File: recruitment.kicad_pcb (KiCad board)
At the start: 2 copper layers, 1 part

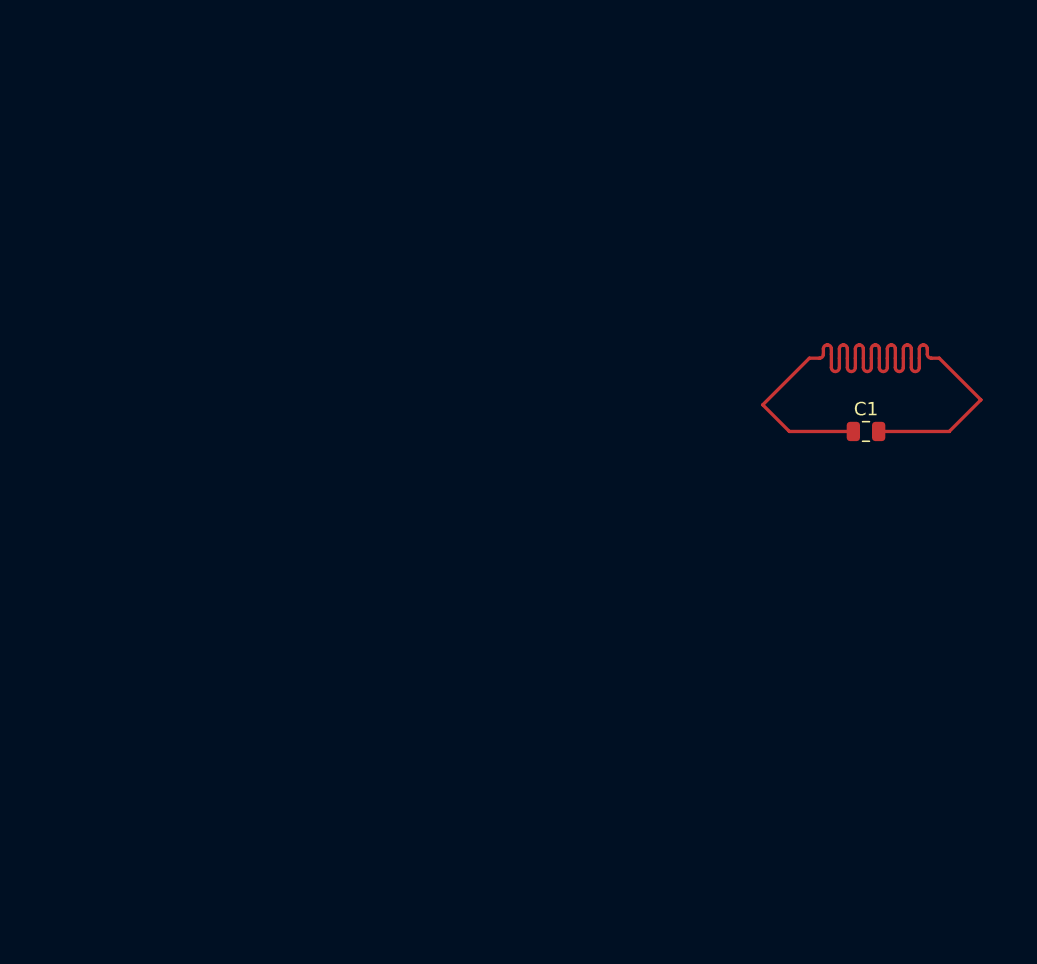
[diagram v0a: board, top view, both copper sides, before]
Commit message: TODO: ad633 footprint
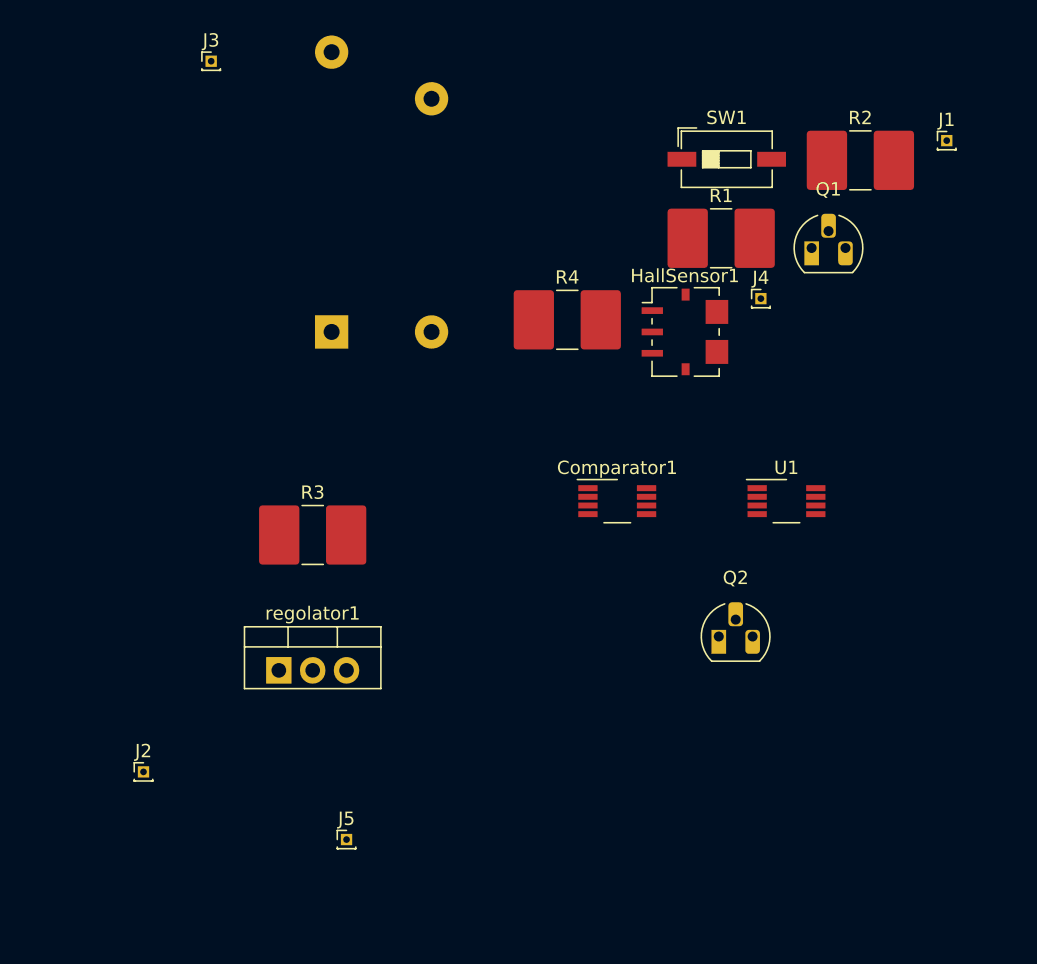
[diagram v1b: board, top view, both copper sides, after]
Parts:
- removed C1: 1F, Capacitor_SMD:C_0805_2012Metric
- added Comparator1: LM393, Package_SO:VSSOP-8_3.0x3.0mm_P0.65mm, F.Cu at (132.1, 94.0)
- added HallSensor1: Allegro ACS781xLR, Sensor_Current:Allegro_PSOF-7_4.8x6.4mm_P1.60mm, F.Cu at (137.2, 81.3)
- added J1: Conn_01x01_Female, Connector_PinHeader_1.00mm:PinHeader_1x01_P1.00mm_Vertical, F.Cu at (156.8, 66.9)
- added J2: Conn_01x01_Female, Connector_PinHeader_1.00mm:PinHeader_1x01_P1.00mm_Vertical, F.Cu at (96.5, 114.3)
- added J3: Conn_01x01_Female, Connector_PinHeader_1.00mm:PinHeader_1x01_P1.00mm_Vertical, F.Cu at (101.6, 61.0)
- added J4: Conn_01x01_Female, Connector_PinHeader_1.00mm:PinHeader_1x01_P1.00mm_Vertical, F.Cu at (142.9, 78.8)
- added J5: Conn_01x01_Female, Connector_PinHeader_1.00mm:PinHeader_1x01_P1.00mm_Vertical, F.Cu at (111.8, 119.4)
- added K1: relay, Relay_THT:Relay_1P1T_NO_10x24x18.8mm_Panasonic_ADW11xxxxW_THT, B.Cu at (110.6, 81.3)
- added Q1: Q_NPN_BCE, Package_TO_SOT_THT:TO-92_HandSolder, F.Cu at (146.7, 75.0)
- added Q2: Q_NPN_BCE, Package_TO_SOT_THT:TO-92_HandSolder, F.Cu at (139.7, 104.1)
- added R1: 1150, Resistor_SMD:R_2816_7142Metric, F.Cu at (139.9, 74.2)
- added R2: 1000, Resistor_SMD:R_2816_7142Metric, F.Cu at (150.3, 68.4)
- added R3: R, Resistor_SMD:R_2816_7142Metric, F.Cu at (109.2, 96.5)
- added R4: R, Resistor_SMD:R_2816_7142Metric, F.Cu at (128.3, 80.4)
- added SW1: SW_SPST, Button_Switch_SMD:SW_DIP_SPSTx01_Slide_6.7x4.1mm_W6.73mm_P2.54mm_LowProfile_JPin, F.Cu at (140.3, 68.3)
- added U1: LM393, Package_SO:VSSOP-8_3.0x3.0mm_P0.65mm, F.Cu at (144.8, 94.0)
- added regolator1: 5V, Package_TO_SOT_THT:TO-220-3_Vertical, F.Cu at (106.7, 106.7)
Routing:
- net Net-(C1-Pad1): track 57.5 -> 0.00 mm

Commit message: footprints/autorouting done, TODO: understand transistor and optimize pcb shape
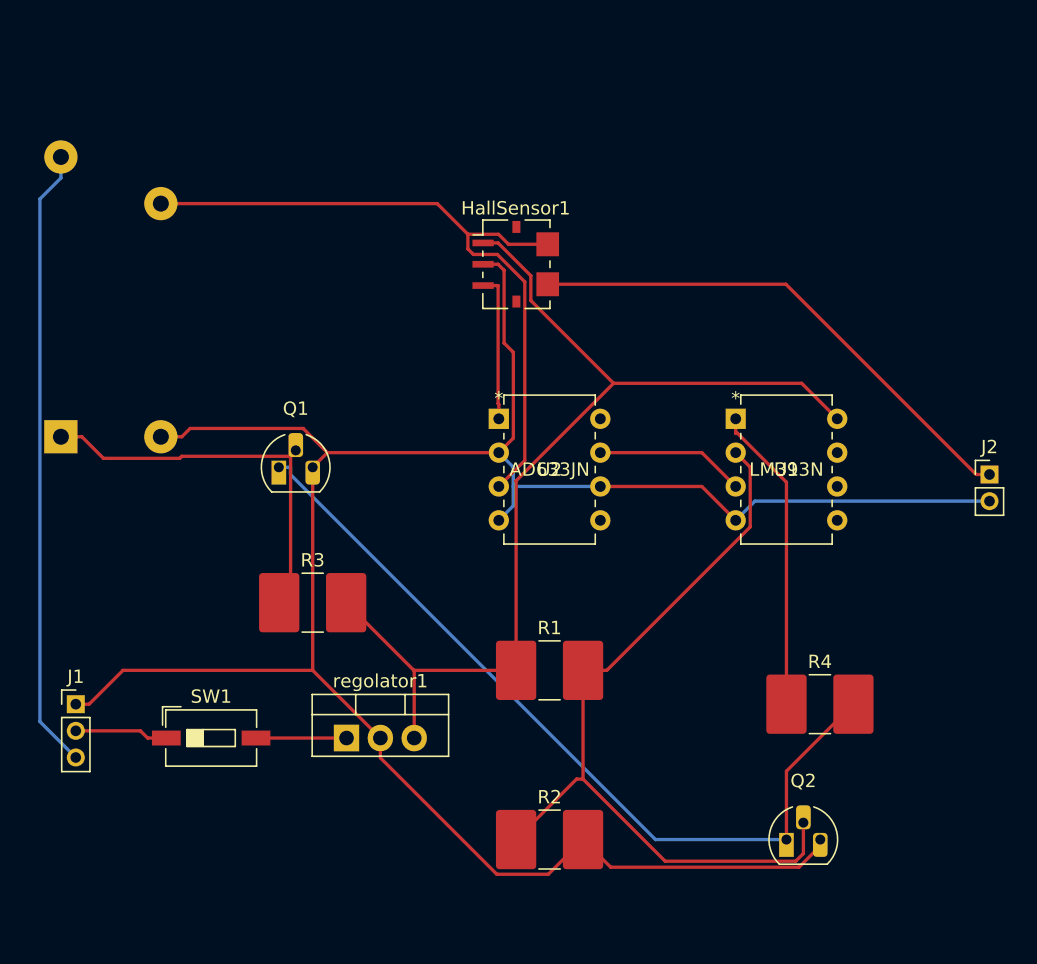
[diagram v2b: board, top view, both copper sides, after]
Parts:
- removed Comparator1: LM393, Package_SO:VSSOP-8_3.0x3.0mm_P0.65mm
- removed J3, J4, J5: Conn_01x01_Female, Connector_PinHeader_1.00mm:PinHeader_1x01_P1.00mm_Vertical
- added U2: AD633JN, LM393:LM393N, F.Cu at (123.2, 87.8)
- J1: value Conn_01x01_Female -> Conn_01x03_Female; footprint Connector_PinHeader_1.00mm:PinHeader_1x01_P1.00mm_Vertical -> Connector_PinHeader_2.00mm:PinHeader_1x03_P2.00mm_Vertical
- J2: value Conn_01x01_Female -> Conn_01x02_Female; footprint Connector_PinHeader_1.00mm:PinHeader_1x01_P1.00mm_Vertical -> Connector_PinHeader_2.00mm:PinHeader_1x02_P2.00mm_Vertical
- U1: value LM393 -> LM393N; footprint Package_SO:VSSOP-8_3.0x3.0mm_P0.65mm -> LM393:LM393N
- moved J1 77.9 mm to (91.4, 109.2)
- moved J2 67.3 mm to (160.0, 92.0)
- moved SW1 58.2 mm to (101.6, 111.8)
- moved R2 56.1 mm to (127.0, 119.4)
- moved Q1 43.2 mm to (106.7, 91.4)
- moved R1 34.9 mm to (127.0, 106.7)
- moved R4 34.5 mm to (147.3, 109.2)
- moved K1 21.8 mm to (90.3, 89.1)
- moved Q2 16.1 mm to (144.8, 119.4)
- moved HallSensor1 13.7 mm to (124.5, 76.2)
- moved U1 7.26 mm to (141.0, 87.8)
- moved regolator1 7.18 mm to (111.8, 111.8)
- moved R3 5.08 mm to (109.2, 101.6)
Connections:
- J1 pad 1: Net-(J1-Pad1) -> GND
- J2 pad 1: GND -> Net-(HallSensor1-Pad5)
- K1 pad 3: Net-(J3-Pad1) -> Net-(J1-Pad3)
- Q2 pad 2: Net-(Comparator1-Pad2) -> Net-(Q2-Pad2)
- R1 pad 2: Net-(Comparator1-Pad2) -> Net-(Q2-Pad2)
- R2 pad 1: Net-(Comparator1-Pad2) -> Net-(Q2-Pad2)
- SW1 pad 1: Net-(J1-Pad1) -> Net-(J1-Pad2)
- U1 pad 1: (no net) -> Net-(R4-Pad1)
- U1 pad 2: (no net) -> Net-(Q2-Pad2)
- U1 pad 3: (no net) -> Net-(U1-Pad3)
- U1 pad 5: (no net) -> unconnected-(U1-Pad5)
- U1 pad 6: (no net) -> unconnected-(U1-Pad6)
- U1 pad 7: (no net) -> unconnected-(U1-Pad7)
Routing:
- net GND: track 0.00 -> 170.0 mm
- net Net-(HallSensor1-Pad1): track 0.00 -> 77.7 mm
- net Net-(Q1-Pad1): track 0.00 -> 62.2 mm
- net Net-(Q2-Pad2): track 0.00 -> 59.8 mm
- net Net-(HallSensor1-Pad6): track 0.00 -> 52.9 mm
- net Net-(J1-Pad3): track 0.00 -> 46.8 mm
- net Net-(HallSensor1-Pad5): track 0.00 -> 39.1 mm
- net Net-(K1-Pad1): track 0.00 -> 29.9 mm
- net Net-(R4-Pad1): track 0.00 -> 23.1 mm
- net Net-(U1-Pad3): track 0.00 -> 11.2 mm
- net Net-(HallSensor1-Pad3): track 0.00 -> 11.1 mm
- net Net-(J1-Pad2): track 0.00 -> 7.02 mm
- net Net-(SW1-Pad2): track 0.00 -> 6.80 mm

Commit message: better shape + MOSFET, TODO: adjust multiplier, it's better AD534
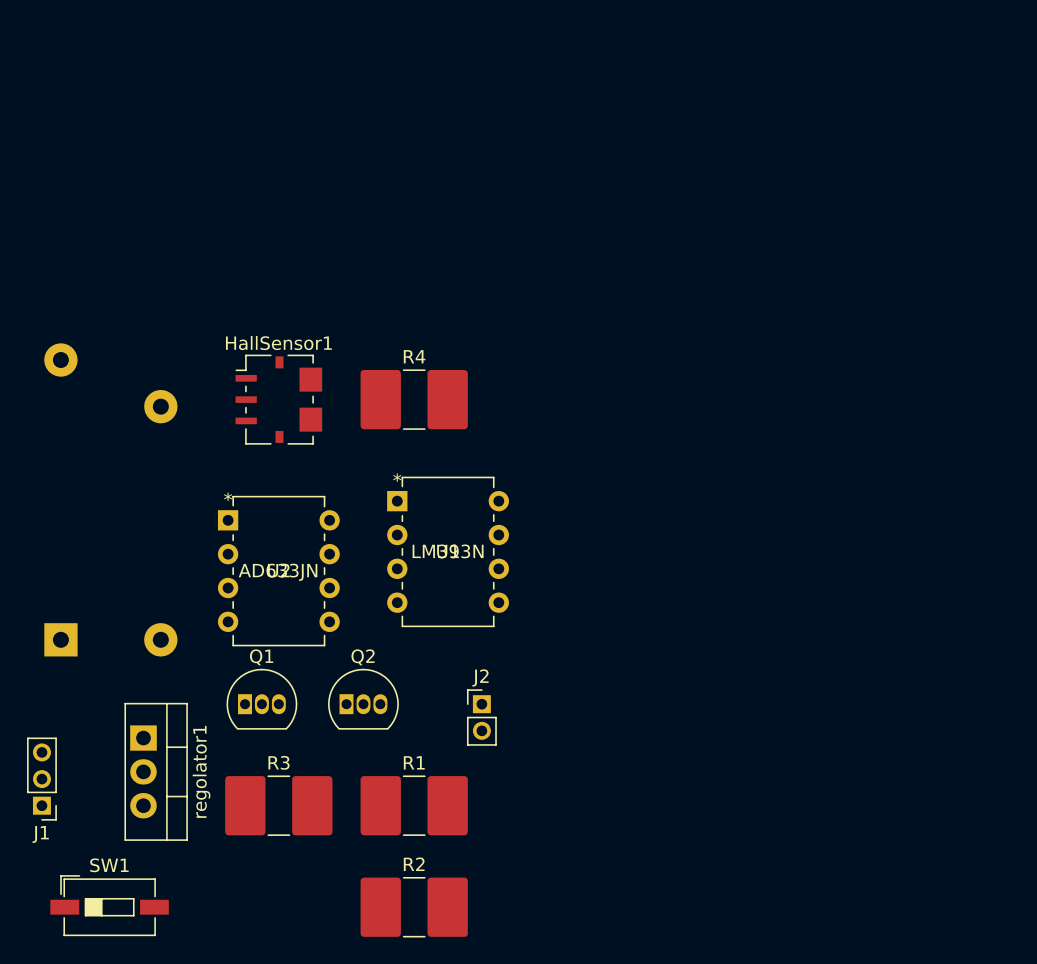
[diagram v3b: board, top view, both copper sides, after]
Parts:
- Q1, Q2: value Q_NPN_BCE -> BS170; footprint Package_TO_SOT_THT:TO-92_HandSolder -> Package_TO_SOT_THT:TO-92_Inline
- moved J2 41.8 mm to (121.9, 109.2)
- moved R4 38.1 mm to (116.8, 86.4)
- moved Q2 34.5 mm to (111.8, 109.2)
- moved U1 26.1 mm to (115.6, 94.0)
- moved U2 21.7 mm to (102.9, 95.4)
- moved HallSensor1 20.5 mm to (106.7, 86.4)
- moved Q1 18.0 mm to (104.1, 109.2)
- moved R3 15.5 mm to (106.7, 116.8)
- moved K1 15.2 mm to (90.3, 104.4)
- moved regolator1 15.2 mm to (96.5, 111.8), turned to -90 degrees
- moved SW1 14.8 mm to (94.0, 124.5)
- moved R1 14.4 mm to (116.8, 116.8)
- moved R2 11.4 mm to (116.8, 124.5)
- moved J1 8.03 mm to (88.9, 116.8), turned to 180 degrees
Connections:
- Q1 pad 1: Net-(Q1-Pad1) -> GND
- Q1 pad 2: Net-(K1-Pad1) -> Net-(R4-Pad2)
- Q1 pad 3: GND -> Net-(K1-Pad1)
- Q2 pad 1: Net-(Q1-Pad1) -> GND
- Q2 pad 2: Net-(Q2-Pad2) -> Net-(R4-Pad2)
- Q2 pad 3: GND -> Net-(R1-Pad2)
- R1 pad 2: Net-(Q2-Pad2) -> Net-(R1-Pad2)
- R2 pad 1: Net-(Q2-Pad2) -> Net-(R1-Pad2)
- R4 pad 2: Net-(Q1-Pad1) -> Net-(R4-Pad2)
- U1 pad 2: Net-(Q2-Pad2) -> Net-(R1-Pad2)
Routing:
- net GND: track 170.0 -> 0.00 mm
- net Net-(HallSensor1-Pad1): track 77.7 -> 0.00 mm
- net Net-(Q1-Pad1): track 62.2 -> 0.00 mm
- net Net-(Q2-Pad2): track 59.8 -> 0.00 mm
- net Net-(HallSensor1-Pad6): track 52.9 -> 0.00 mm
- net Net-(J1-Pad3): track 46.8 -> 0.00 mm
- net Net-(HallSensor1-Pad5): track 39.1 -> 0.00 mm
- net Net-(K1-Pad1): track 29.9 -> 0.00 mm
- net Net-(R4-Pad1): track 23.1 -> 0.00 mm
- net Net-(U1-Pad3): track 11.2 -> 0.00 mm
- net Net-(HallSensor1-Pad3): track 11.1 -> 0.00 mm
- net Net-(J1-Pad2): track 7.02 -> 0.00 mm
- net Net-(SW1-Pad2): track 6.80 -> 0.00 mm

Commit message: correct multiplier, TODO: check MOSFET
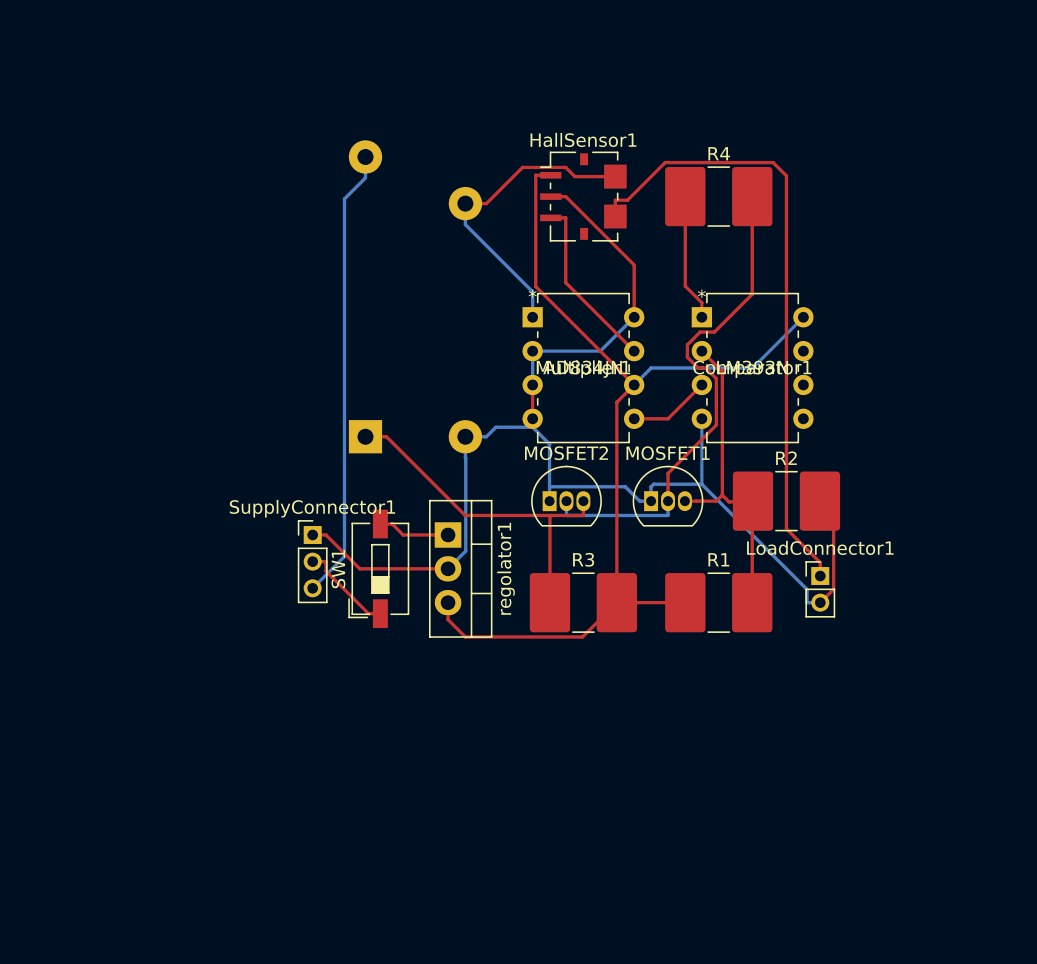
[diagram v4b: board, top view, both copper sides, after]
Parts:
- removed J1: Conn_01x03_Female, Connector_PinHeader_2.00mm:PinHeader_1x03_P2.00mm_Vertical
- removed J2: Conn_01x02_Female, Connector_PinHeader_2.00mm:PinHeader_1x02_P2.00mm_Vertical
- removed K1: relay, Relay_THT:Relay_1P1T_NO_10x24x18.8mm_Panasonic_ADW11xxxxW_THT
- removed Q1, Q2: BS170, Package_TO_SOT_THT:TO-92_Inline
- removed U1: LM393N, LM393:LM393N
- removed U2: AD633JN, LM393:LM393N
- added Comparator1: LM393N, LM393:LM393N, F.Cu at (138.4, 80.2)
- added LoadConnector1: Conn_01x02_Female, Connector_PinHeader_2.00mm:PinHeader_1x02_P2.00mm_Vertical, F.Cu at (147.3, 99.6)
- added MOSFET1: BS170, Package_TO_SOT_THT:TO-92_Inline, F.Cu at (134.6, 94.0)
- added MOSFET2: BS170, Package_TO_SOT_THT:TO-92_Inline, F.Cu at (127.0, 94.0)
- added Multiplier1: AD834JN, LM393:LM393N, F.Cu at (125.7, 80.2)
- added Relay1: relay, Relay_THT:Relay_1P1T_NO_10x24x18.8mm_Panasonic_ADW11xxxxW_THT, B.Cu at (113.2, 89.1)
- added SupplyConnector1: Conn_01x03_Female, Connector_PinHeader_2.00mm:PinHeader_1x03_P2.00mm_Vertical, F.Cu at (109.2, 96.5)
- moved R2 41.3 mm to (144.8, 94.0)
- moved SW1 32.5 mm to (114.3, 99.1), turned to 90 degrees
- moved regolator1 27.5 mm to (119.4, 96.5)
- moved R1 27.5 mm to (139.7, 101.6)
- moved R3 27.5 mm to (129.5, 101.6)
- moved HallSensor1 27.5 mm to (129.5, 71.1)
- moved R4 27.5 mm to (139.7, 71.1)
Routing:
- net GND: track 0.00 -> 99.4 mm
- net Net-(HallSensor1-Pad1): track 0.00 -> 72.3 mm
- net Net-(HallSensor1-Pad5): track 0.00 -> 46.7 mm
- net Net-(MOSFET2-Pad2): track 0.00 -> 38.0 mm
- net Net-(SupplyConnector1-Pad3): track 0.00 -> 34.0 mm
- net Net-(Relay1-Pad1): track 0.00 -> 26.4 mm
- net Net-(MOSFET1-Pad3): track 0.00 -> 24.5 mm
- net Net-(HallSensor1-Pad6): track 0.00 -> 23.3 mm
- net Net-(HallSensor1-Pad3): track 0.00 -> 13.3 mm
- net Net-(R4-Pad1): track 0.00 -> 9.57 mm
- net Net-(SupplyConnector1-Pad2): track 0.00 -> 7.11 mm
- net Net-(Comparator1-Pad3): track 0.00 -> 6.13 mm
- net Net-(SW1-Pad2): track 0.00 -> 5.42 mm

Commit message: routing, first release
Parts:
- removed MOSFET1, MOSFET2: BS170, Package_TO_SOT_THT:TO-92_Inline
- removed Multiplier1: AD834JN, LM393:LM393N
- removed R1: 1150, Resistor_SMD:R_2816_7142Metric
- removed R2: 1000, Resistor_SMD:R_2816_7142Metric
- removed R3, R4: R, Resistor_SMD:R_2816_7142Metric
- added Q1: BSN20, Package_TO_SOT_SMD:SOT-23, F.Cu at (121.9, 88.9)
- added Rhall1: 90, Resistor_SMD:R_2816_7142Metric, F.Cu at (134.6, 76.2)
- added Rhall2: 10, Resistor_SMD:R_2816_7142Metric, F.Cu at (134.6, 83.8)
- added Rload1: 9900, Resistor_SMD:R_2816_7142Metric, F.Cu at (144.8, 76.2)
- added Rload2: 100, Resistor_SMD:R_2816_7142Metric, F.Cu at (144.8, 83.8)
- added Rref1: 4000, Resistor_SMD:R_2816_7142Metric, F.Cu at (129.5, 106.7)
- added Rref2: 10, Resistor_SMD:R_2816_7142Metric, F.Cu at (139.7, 106.7)
- added Rrelay1: R, Resistor_SMD:R_2816_7142Metric, F.Cu at (124.5, 94.0)
- added Rrelay2: R, Resistor_SMD:R_2816_7142Metric, F.Cu at (124.5, 83.8)
- added flipflop1: 74HC74PW-Q100_118, footprints:74HC74PW-Q100_118, F.Cu at (149.9, 106.7)
- added multiplier1: AD835AN, ad835:AD835AN, F.Cu at (143.5, 90.2)
- moved LoadConnector1 23.9 mm to (152.4, 76.2)
- moved Comparator1 12.7 mm to (130.8, 90.3)
- moved SupplyConnector1 10.2 mm to (109.2, 106.7), turned to 180 degrees
- moved HallSensor1 7.18 mm to (124.5, 76.2)
- moved Relay1 5.68 mm to (110.6, 94.2)
- moved SW1 5.08 mm to (114.3, 104.1)
- moved regolator1 5.08 mm to (119.4, 101.6)
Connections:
- net Net-(HallSensor1-Pad1) renamed /Vcc
- Comparator1 pad 1: Net-(R4-Pad1) -> /V_comp
- Comparator1 pad 2: Net-(MOSFET1-Pad3) -> /V_ref
- Comparator1 pad 3: Net-(Comparator1-Pad3) -> unconnected-(Comparator1-Pad3)
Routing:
- net /V_ff: track 0.00 -> 41.9 mm
- net GND: track 99.4 -> 140.5 mm
- net Net-(MOSFET2-Pad2): track 38.0 -> 0.00 mm
- net /V_Nhall: track 0.00 -> 37.6 mm
- net /Vcc: track 72.3 -> 106.2 mm
- net /V_ref: track 0.00 -> 29.6 mm
- net Net-(MOSFET1-Pad3): track 24.5 -> 0.00 mm
- net /V_comp: track 0.00 -> 24.0 mm
- net /V_Nload: track 0.00 -> 16.6 mm
- net Net-(HallSensor1-Pad5): track 46.7 -> 31.9 mm
- net Net-(HallSensor1-Pad6): track 23.3 -> 10.9 mm
- net Net-(Rrelay1-Pad1): track 26.4 -> 15.9 mm
- net Net-(R4-Pad1): track 9.57 -> 0.00 mm
- net Net-(Comparator1-Pad3): track 6.13 -> 0.00 mm
- net Net-(Rrelay2-Pad1): track 0.00 -> 5.46 mm
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
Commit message: check
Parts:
- removed LoadConnector1: Conn_01x02_Female, Connector_PinHeader_2.00mm:PinHeader_1x02_P2.00mm_Vertical
- removed SupplyConnector1: Conn_01x03_Female, Connector_PinHeader_2.00mm:PinHeader_1x03_P2.00mm_Vertical
- added LoadConnect1: Conn_01x02_Female, Connector_PinHeader_2.00mm:PinHeader_1x02_P2.00mm_Vertical, F.Cu at (154.9, 83.8)
- added SupplyConnect1: Conn_01x03_Female, Connector_PinHeader_2.00mm:PinHeader_1x03_P2.00mm_Vertical, F.Cu at (111.8, 109.2)
- Rrelay1: value R -> 10
- Rrelay2: value R -> 15
- SW1: value SW_SPST -> switch
- moved Rload2 5.70 mm to (147.3, 88.9)
- moved Rhall2 5.68 mm to (137.2, 88.9)
- moved multiplier1 5.68 mm to (146.1, 95.2)
- moved HallSensor1 5.68 mm to (127.0, 81.3)
- moved Relay1 5.68 mm to (113.2, 99.3)
- moved Rrelay1 5.68 mm to (127.0, 99.1)
- moved SW1 5.68 mm to (116.8, 109.2)
- moved Comparator1 5.68 mm to (133.3, 95.4)
- moved Q1 5.68 mm to (124.5, 94.0)
- moved Rhall1 5.68 mm to (137.2, 81.3)
- moved Rrelay2 5.67 mm to (127.0, 88.9)
- moved Rload1 5.67 mm to (147.3, 81.3)
- moved regolator1 5.24 mm to (121.9, 106.2)
- moved Rref1 3.61 mm to (132.1, 109.2)
- moved Rref2 3.59 mm to (142.2, 109.2)
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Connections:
- Comparator1 pad 3: unconnected-(Comparator1-Pad3) -> /V_pot
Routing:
- net GND: track 140.5 -> 114.2 mm
- net /V_pot: track 0.00 -> 22.2 mm
- net /Vcc: track 106.2 -> 86.2 mm, vias 0 -> 1
- net /V_Nhall: track 37.6 -> 27.4 mm, vias 0 -> 1
- net /V_ff: track 41.9 -> 48.0 mm
- net Net-(SW1-Pad1): track 6.25 -> 10.4 mm
- net Net-(HallSensor1-Pad3): track 16.7 -> 20.4 mm
- net Net-(Relay1-Pad3): track 30.2 -> 27.6 mm
- net /V_ref: track 29.6 -> 27.1 mm
- net Net-(HallSensor1-Pad5): track 31.9 -> 34.1 mm
- net Net-(HallSensor1-Pad6): track 10.9 -> 9.56 mm
